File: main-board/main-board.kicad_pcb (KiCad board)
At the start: 2 copper layers, 48 parts, among them J1 INPUT, J2 NC1, J3 OUTPUT, J4 Conn_01x03_Pin, J5 COM, J6 Conn_01x03_Pin, SW1 SW_SPST, U1 ADA4898-2, U2 ADA4898-2, U3 AD633ANZ

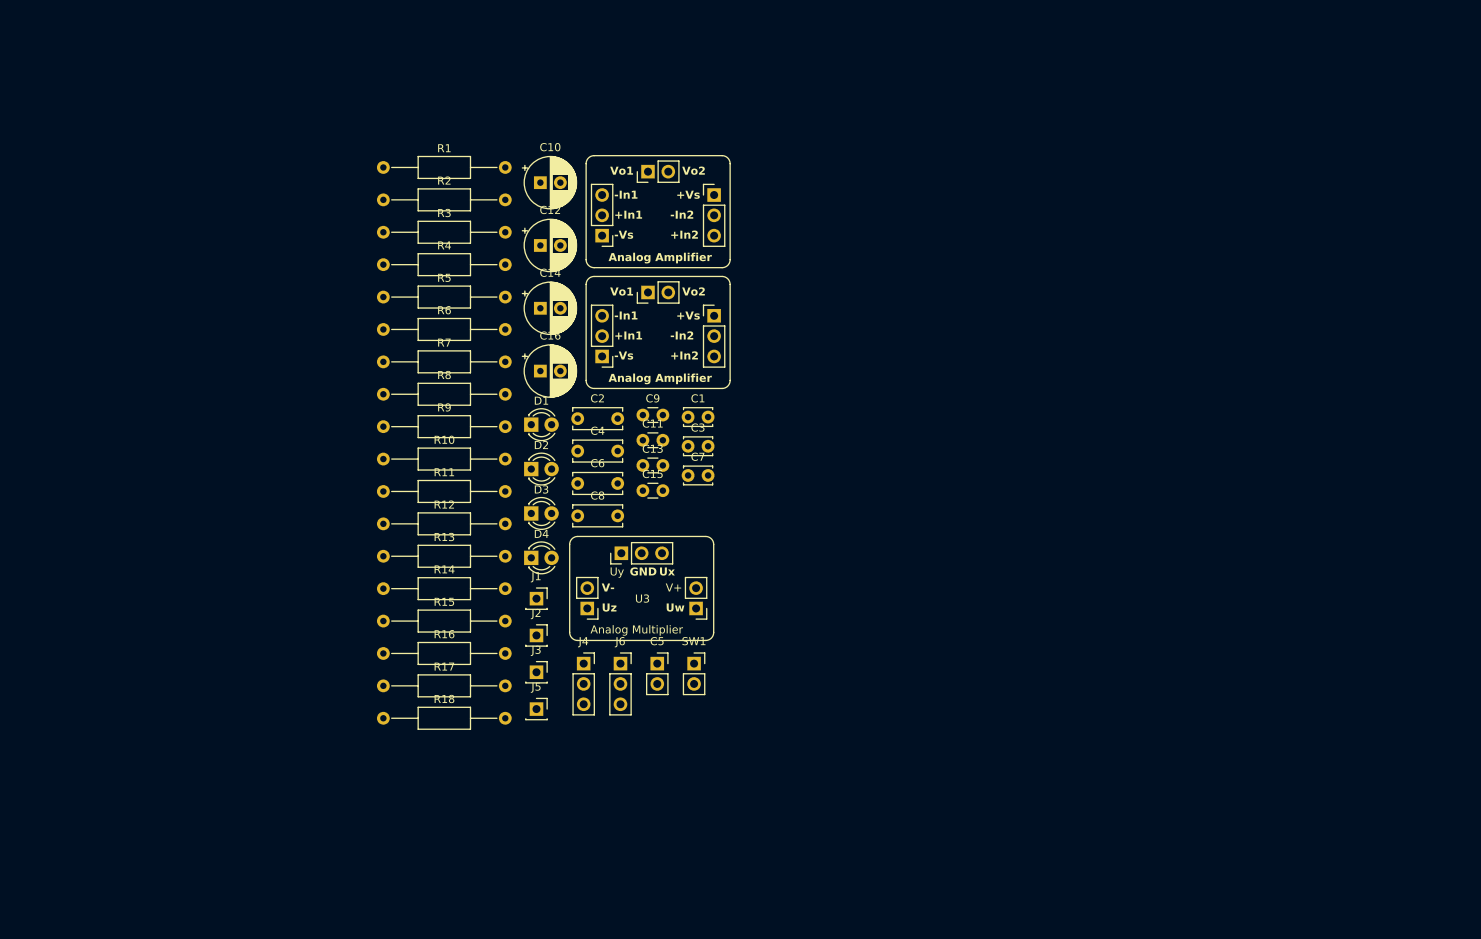
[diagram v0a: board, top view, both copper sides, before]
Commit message: Adjust main board footprints and pcb layout
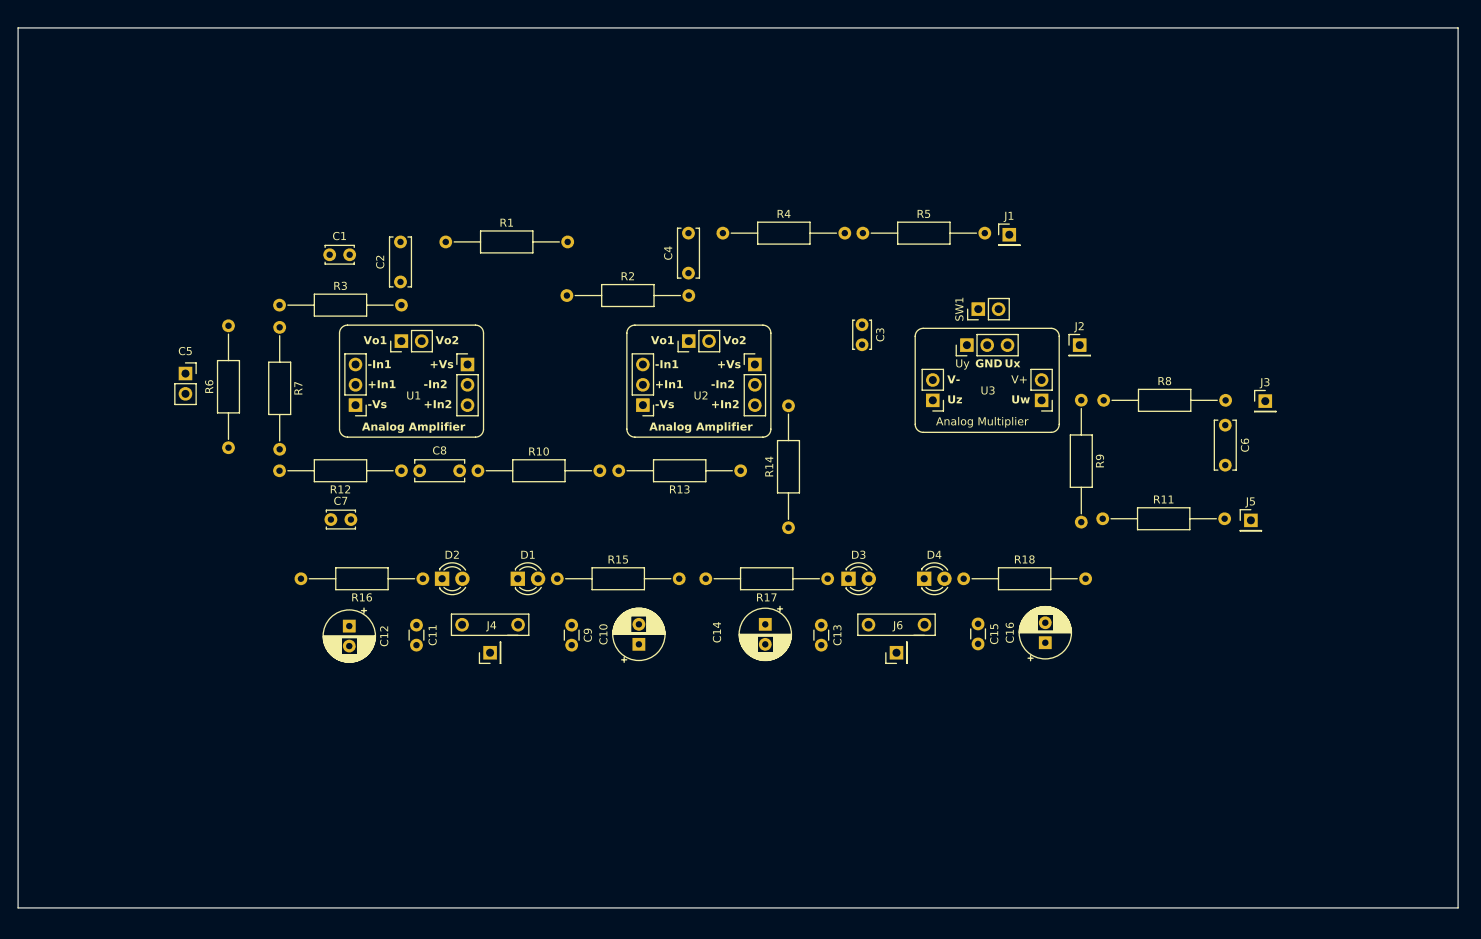
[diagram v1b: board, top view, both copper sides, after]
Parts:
- C5: footprint Connector_PinSocket_2.54mm:PinSocket_1x02_P2.54mm_Vertical -> footprints:CapacitorSocket
- J1, J2, J3, J5: footprint Connector_PinSocket_2.54mm:PinSocket_1x01_P2.54mm_Vertical -> Connector_PinHeader_2.54mm:PinHeader_1x01_P2.54mm_Vertical
- J4, J6: footprint Connector_PinSocket_2.54mm:PinSocket_1x03_P2.54mm_Vertical -> footprints:PowerHeader
- SW1: footprint Connector_PinSocket_2.54mm:PinSocket_1x02_P2.54mm_Vertical -> footprints:Switch
- moved J3 97.2 mm to (215.9, 89.7)
- moved J5 92.4 mm to (214.1, 104.5)
- moved R8 90.0 mm to (195.7, 89.5)
- moved R11 90.0 mm to (195.6, 104.3)
- moved R9 87.3 mm to (192.9, 89.5), turned to -90 degrees
- moved C6 81.3 mm to (210.9, 92.7), turned to -90 degrees
- moved J2 77.0 mm to (192.7, 82.7)
- moved R18 74.6 mm to (178.2, 111.8)
- moved J1 74.6 mm to (183.9, 68.8)
- moved C16 71.7 mm to (188.4, 119.8), turned to 90 degrees
- moved C5 69.2 mm to (80.9, 86.2)
- moved R5 60.5 mm to (165.6, 68.7)
- moved C10 59.0 mm to (137.6, 120.0), turned to 90 degrees
- moved R17 57.1 mm to (161.2, 111.8), turned to 180 degrees
- moved SW1 56.8 mm to (180.0, 78.2), turned to 90 degrees
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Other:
- board outline added: 180 x 110 mm

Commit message: Modifies PCB Layout cosmetics
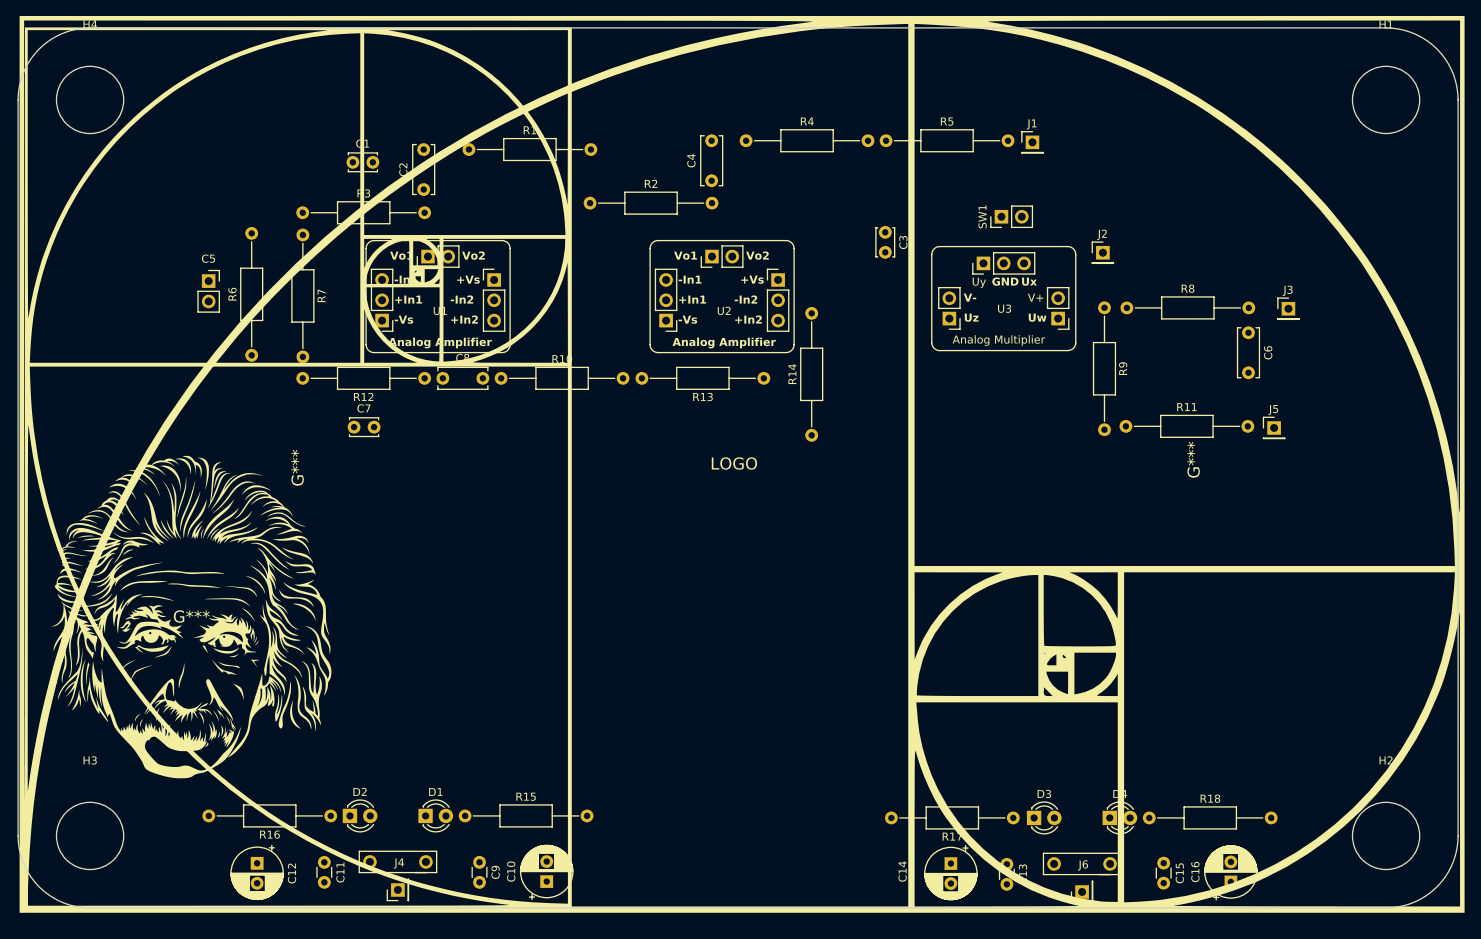
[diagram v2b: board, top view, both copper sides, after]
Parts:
- added G***: LOGO, LOGO, F.Cu at (81.7, 116.6)
- added G***: LOGO, LOGO, F.Cu at (95.0, 98.0)
- added G***: LOGO, LOGO, F.Cu at (150.5, 97.5)
- added G***: LOGO, LOGO, B.Cu at (150.0, 97.5)
- added G***: LOGO, LOGO, B.Cu at (207.0, 97.0)
- added H1: MountingHole, MountingHole:MountingHole_8.4mm_M8, F.Cu at (231.0, 52.0)
- added H2: MountingHole, MountingHole:MountingHole_8.4mm_M8, F.Cu at (231.0, 144.0)
- added H3: MountingHole, MountingHole:MountingHole_8.4mm_M8, F.Cu at (69.0, 144.0)
- added H4: MountingHole, MountingHole:MountingHole_8.4mm_M8, F.Cu at (69.0, 52.0)
- moved D4 37.8 mm to (196.5, 141.8)
- moved R17 37.8 mm to (184.4, 141.8)
- moved R18 37.8 mm to (201.4, 141.8)
- moved C13 37.8 mm to (183.6, 147.6)
- moved C15 37.8 mm to (203.2, 147.4)
- moved C16 37.8 mm to (211.6, 149.8)
- moved D3 37.8 mm to (187.0, 141.8)
- moved J6 37.8 mm to (196.5, 147.5)
- moved C14 37.8 mm to (176.6, 147.4)
- moved R15 31.8 mm to (115.9, 141.5)
- moved C11 31.8 mm to (98.3, 147.3)
- moved C9 31.8 mm to (117.7, 147.3)
- moved D1 31.8 mm to (110.9, 141.5)
- moved D2 31.8 mm to (101.5, 141.5)
- moved J4 31.8 mm to (111.0, 147.2)
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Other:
- outline, holes or cut-outs redrawn

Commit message: Changes 3d files and footprints to match module cosmetic changes
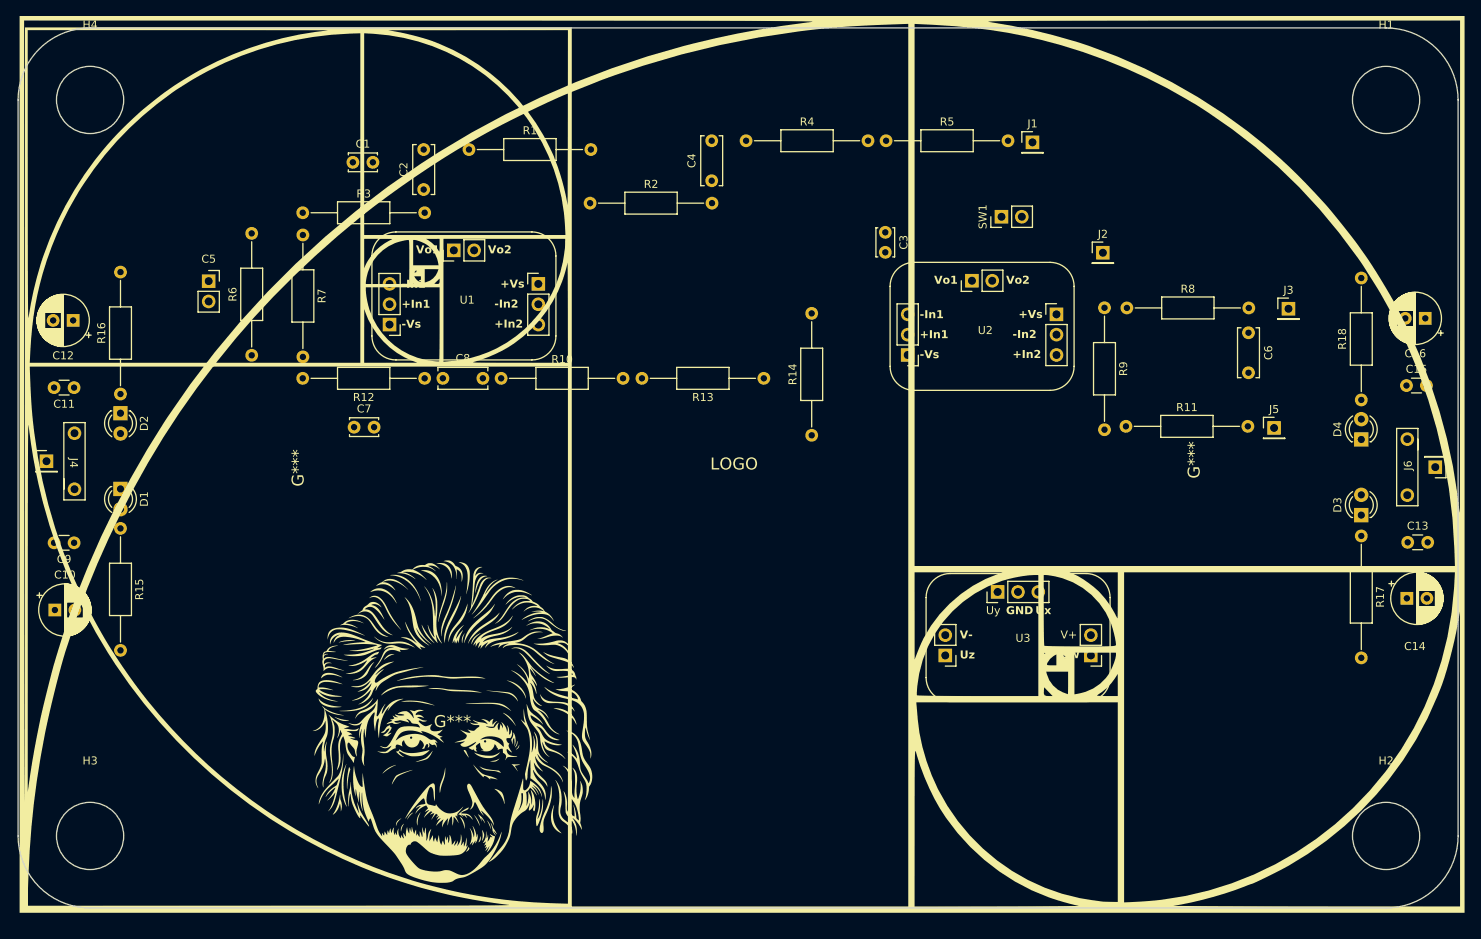
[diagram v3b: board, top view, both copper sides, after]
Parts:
- moved C16 74.5 mm to (235.9, 79.3), turned to 180 degrees
- moved C12 71.6 mm to (66.9, 79.6), turned to 180 degrees
- moved C10 70.2 mm to (64.6, 115.8), turned to 0 degrees
- moved C11 67.1 mm to (67.0, 88.0), turned to 180 degrees
- moved C15 67.0 mm to (233.6, 87.7), turned to 0 degrees
- moved C14 65.9 mm to (233.6, 114.3), turned to 0 degrees
- moved J6 64.8 mm to (233.7, 94.4), turned to 180 degrees
- moved C9 64.5 mm to (67.0, 107.4), turned to 180 degrees
- moved C13 64.3 mm to (233.7, 107.3), turned to 0 degrees
- moved J4 64.0 mm to (67.0, 100.7), turned to 0 degrees
- moved R16 58.9 mm to (72.8, 88.8), turned to 90 degrees
- moved R18 58.6 mm to (227.9, 89.5), turned to 90 degrees
- moved D2 57.9 mm to (72.8, 91.2), turned to -90 degrees
- moved D4 56.8 mm to (227.9, 94.4), turned to 90 degrees
- moved R15 56.1 mm to (72.8, 105.6), turned to -90 degrees
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
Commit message: Modifies Main Board PCB Layout component disposal
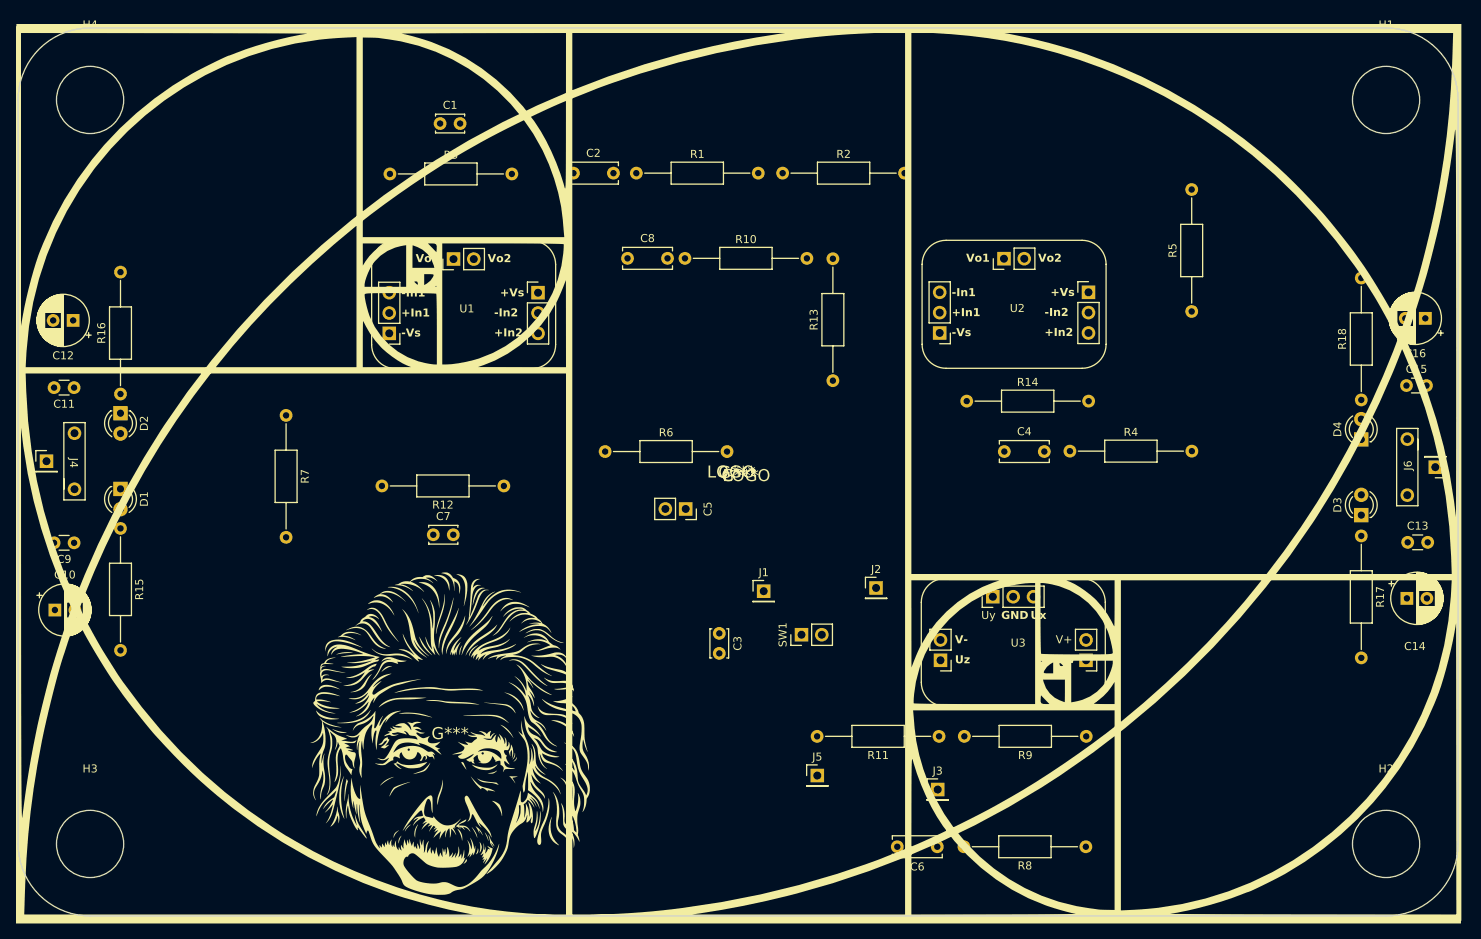
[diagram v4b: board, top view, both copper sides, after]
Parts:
- removed the G*** at (95.0, 98.0)
- removed the G*** at (150.0, 97.5)
- removed the G*** at (207.0, 97.0)
- added G***: LOGO, LOGO, F.Cu at (150.1, 99.0)
- added G***: LOGO, LOGO, B.Cu at (149.8, 98.5)
- added G***: LOGO, LOGO, B.Cu at (150.2, 99.0)
- moved C6 75.1 mm to (174.9, 145.3), turned to 180 degrees
- moved J3 74.4 mm to (174.9, 138.2)
- moved J5 71.8 mm to (159.9, 136.4)
- moved R8 67.5 mm to (193.5, 145.3), turned to 180 degrees
- moved C5 66.1 mm to (143.4, 103.1), turned to -90 degrees
- moved J1 65.4 mm to (153.2, 113.4)
- moved SW1 57.9 mm to (157.9, 118.8)
- moved R4 56.1 mm to (191.5, 95.9)
- moved C3 54.3 mm to (147.7, 118.7)
- moved R9 53.6 mm to (193.5, 131.6), turned to 180 degrees
- moved J2 50.6 mm to (167.2, 113.0)
- moved C4 49.8 mm to (183.3, 96.0), turned to 0 degrees
- moved R6 45.8 mm to (133.4, 96.0), turned to 0 degrees
- moved R11 45.2 mm to (175.1, 131.6), turned to 180 degrees
- moved R5 43.8 mm to (206.7, 78.4), turned to 90 degrees
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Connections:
- net Net-(C2-Pad2) renamed /w5
- net Net-(C4-Pad2) renamed /w11
- net Net-(C8-Pad2) renamed /w6
- net Net-(D1-A) renamed /led_VSS
- net Net-(D2-K) renamed /led_VCC
- net Net-(D3-K) renamed /led_VDD
- net Net-(D4-A) renamed /led_VEE
- net Net-(J1-Pin_1) renamed /w_input
- net Net-(J2-Pin_1) renamed /w_nc
- net Net-(J3-Pin_1) renamed /w_out
- net Net-(U1-+In1) renamed /w_signal+
- net Net-(U1-+In2) renamed /w_signal-
- net Net-(U1--In1) renamed /w1
- net Net-(U1--In2) renamed /w2
- net Net-(U1-Vo1) renamed /w3
- net Net-(U1-Vo2) renamed /w4
- net Net-(U2-+In1) renamed /w8
- net Net-(U2-+In2) renamed /w9
- net Net-(U2--In1) renamed /w7
- net Net-(U2--In2) renamed /w12
- net Net-(U2-Vo1) renamed /w10
- net Net-(U3-Uw) renamed /w13
- net Net-(U3-Uz) renamed /w14
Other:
- board size 180 x 110 mm -> 180 x 111 mm
